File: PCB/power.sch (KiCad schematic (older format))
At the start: 46 parts, among them J801 V_IN, Q801 AOD4189, U801 ACS712xLCTR-20A, U802 NCP1117-5.0_SOT223, U803 L5973D, U804 NCP1117-3.3_SOT223

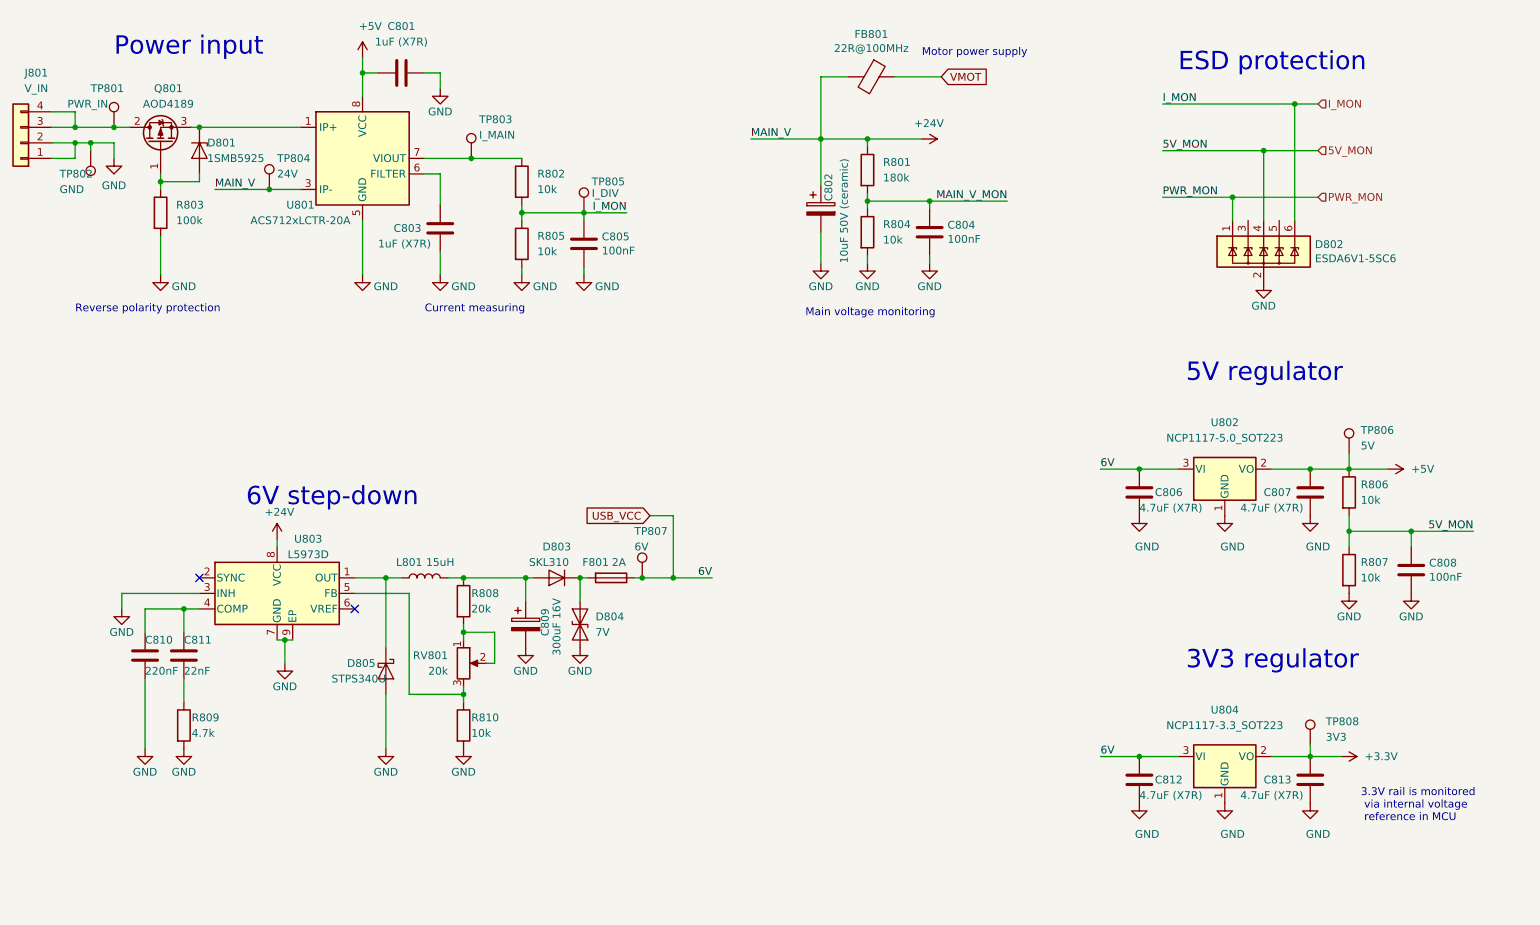
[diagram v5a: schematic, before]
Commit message: Schema: fix schema ERC, connect CS, FLAG and BUSY pins to MCU, connect SPI
ERC: fixed L6470 pin types, add power flags, fixed programming
connector pin types
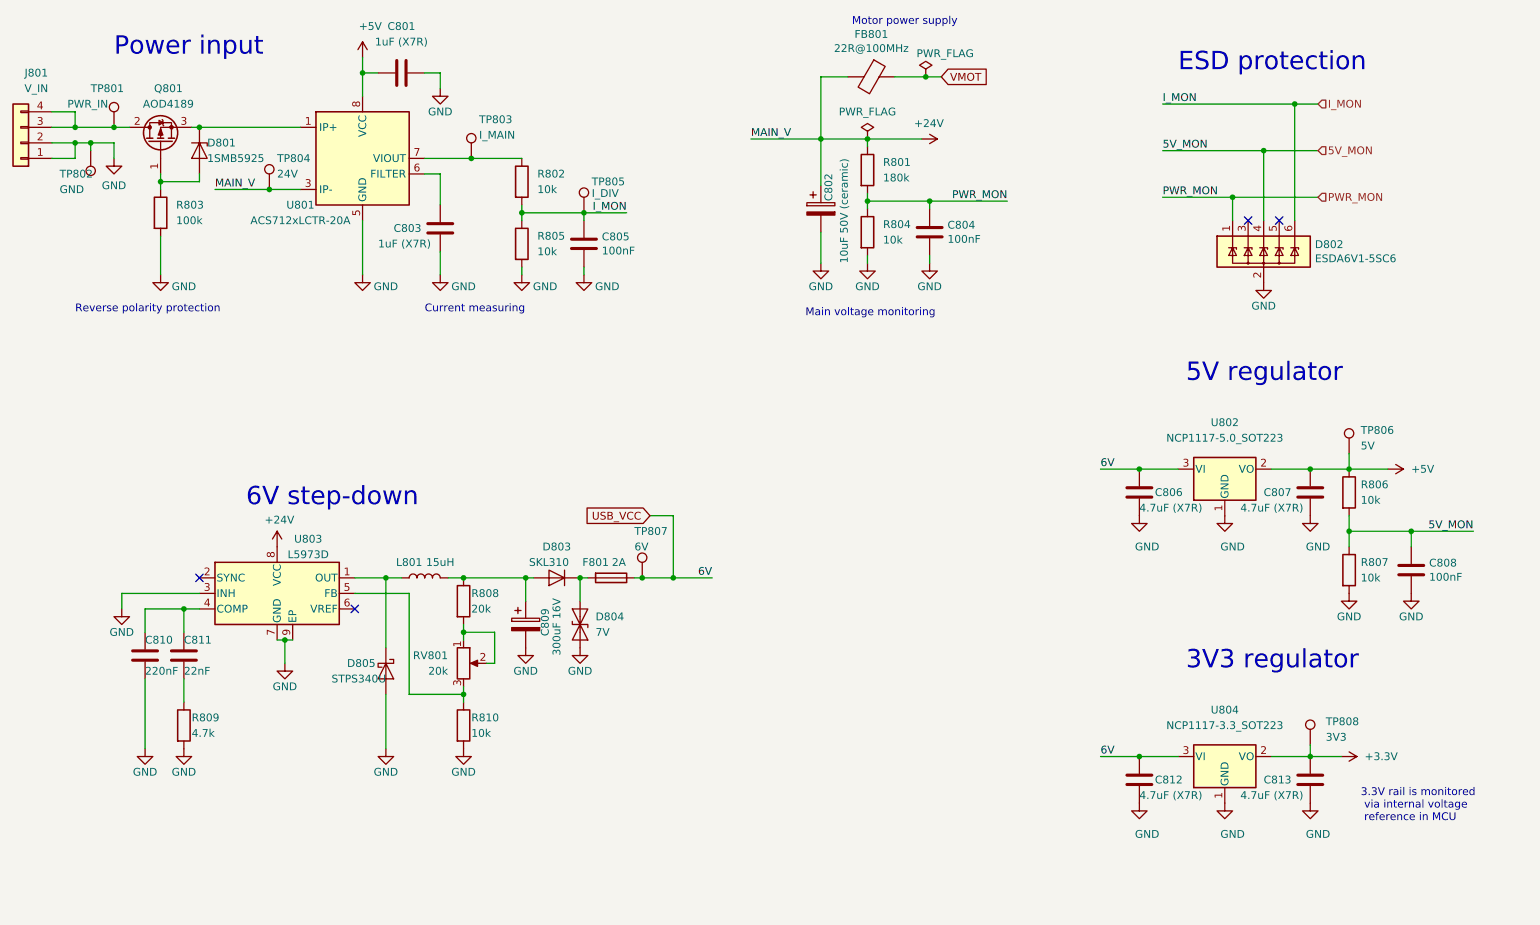
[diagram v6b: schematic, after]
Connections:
- net MAIN_V_MON is gone; now on net PWR_MON: C804.1, R801.2, R804.1
- no-connect marks 2 -> 4
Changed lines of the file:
@@
 	8900 1750 8450 1750
 Connection ~ 8900 1750
-Text Label 7450 1775 2    50   ~ 0
-MAIN_V_MON
-Text Label 8450 1750 0    50   ~ 0
-PWR_MON
 $Comp
 L Device:C C808
@@
 	3700 1500 4000 1500
 Wire Wire Line
-	2750 3950 2750 4000
-Wire Wire Line
 	8450 1150 9300 1150
 Wire Wire Line
@@
 VMOT
 Wire Wire Line
-	6725 975  7025 975
+	6725 975  6925 975
 Wire Wire Line
 	6950 1775 7450 1775
@@
 L power:+24V #PWR0818
 U 1 1 5D4903EF
-P 2750 3950
-F 0 "#PWR0818" H 2750 3800 50  0001 C CNN
-F 1 "+24V" H 2765 4123 50  0000 C CNN
-F 2 "" H 2750 3950 50  0001 C CNN
-F 3 "" H 2750 3950 50  0001 C CNN
-	1    2750 3950
+P 2750 4000
+F 0 "#PWR0818" H 2750 3850 50  0001 C CNN
+F 1 "+24V" H 2765 4173 50  0000 C CNN
+F 2 "" H 2750 4000 50  0001 C CNN
+F 3 "" H 2750 4000 50  0001 C CNN
+	1    2750 4000
 	1    0    0    -1
 $EndComp
@@
 Text Notes 6150 2525 0    50   ~ 0
 Main voltage monitoring
-Text Notes 6900 850  0    50   ~ 0
+Text Notes 6450 650  0    50   ~ 0
 Motor power supply
 Text Notes 3700 2500 0    50   ~ 0
@@
 Text Notes 9725 5775 0    50   ~ 0
 3.3V rail is monitored\n via internal voltage\n reference in MCU
+Text Label 8450 1750 0    50   ~ 0
+PWR_MON
+Text Label 7450 1775 2    50   ~ 0
+PWR_MON
+$Comp
+L power:PWR_FLAG #FLG0107
+U 1 1 5E41C5DC
+P 6925 975
+F 0 "#FLG0107" H 6925 1050 50  0001 C CNN
+F 1 "PWR_FLAG" H 7050 1125 50  0000 C CNN
+F 2 "" H 6925 975 50  0001 C CNN
+F 3 "~" H 6925 975 50  0001 C CNN
+	1    6925 975
+	1    0    0    -1
+$EndComp
+Connection ~ 6925 975
+Wire Wire Line
+	6925 975  7025 975
+NoConn ~ 9000 1900
+NoConn ~ 9200 1900
+$Comp
+L power:PWR_FLAG #FLG0109
+U 1 1 5E439F29
+P 6550 1375
+F 0 "#FLG0109" H 6550 1450 50  0001 C CNN
+F 1 "PWR_FLAG" H 6550 1550 50  0000 C CNN
+F 2 "" H 6550 1375 50  0001 C CNN
+F 3 "~" H 6550 1375 50  0001 C CNN
+	1    6550 1375
+	1    0    0    -1
+$EndComp
 $EndSCHEMATC

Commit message: PCB: route current meter, reverse polarity protection, stepdown converter
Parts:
- D802: footprint Package_TO_SOT_SMD:SOT-23-6 -> Package_DFN_QFN:ST_UQFN-6L_1.5x1.7mm_Pitch0.5mm
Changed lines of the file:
@@
 F 0 "D802" H 9430 2146 50  0000 L CNN
 F 1 "ESDA6V1-5SC6" H 9430 2055 50  0000 L CNN
-F 2 "Package_TO_SOT_SMD:SOT-23-6" H 9800 1850 50  0001 C CNN
+F 2 "Package_DFN_QFN:ST_UQFN-6L_1.5x1.7mm_Pitch0.5mm" H 9800 1850 50  0001 C CNN
 F 3 "www.st.com/resource/en/datasheet/esda6v1-5sc6.pdf" V 9100 2100 50  0001 C CNN
 	1    9100 2100

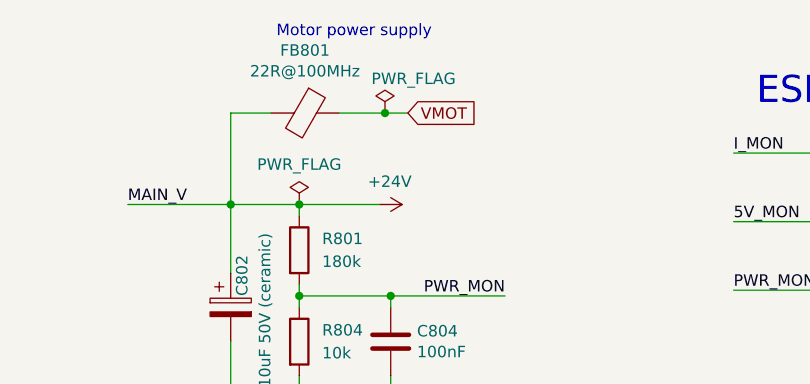
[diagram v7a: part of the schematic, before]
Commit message: PCB: upgrade power lines for VMOT (3mm -> 5mm), add second ferrite to VMOT
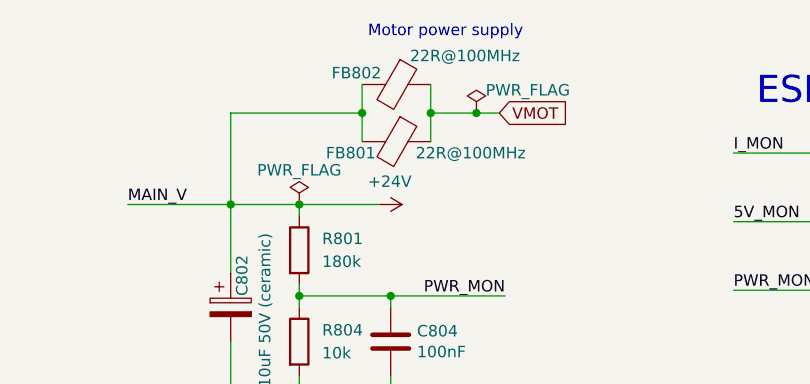
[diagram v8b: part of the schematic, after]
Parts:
- added FB802: 22R@100MHz, Inductor_SMD:L_0805_2012Metric, symbol Device:Ferrite_Bead
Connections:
- net +24V: now also FB802.2
- net VMOT: now also FB802.1
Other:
- moved on the sheet: FB801
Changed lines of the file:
@@
 L Device:Ferrite_Bead FB801
 U 1 1 5D478B04
-P 6575 975
-F 0 "FB801" V 6301 975 50  0000 C CNN
-F 1 "22R@100MHz" V 6392 975 50  0000 C CNN
-F 2 "Inductor_SMD:L_0805_2012Metric" V 6505 975 50  0001 C CNN
-F 3 "~" H 6575 975 50  0001 C CNN
-	1    6575 975
+P 6975 850
+F 0 "FB801" V 7275 650 50  0000 C CNN
+F 1 "22R@100MHz" V 7275 1175 50  0000 C CNN
+F 2 "Inductor_SMD:L_0805_2012Metric" V 6905 850 50  0001 C CNN
+F 3 "~" H 6975 850 50  0001 C CNN
+	1    6975 850
 	0    1    1    0
 $EndComp
-Text GLabel 7025 975  2    50   Input ~ 0
+Text GLabel 7425 975  2    50   Input ~ 0
 VMOT
 Wire Wire Line
-	6725 975  6925 975
+	7125 975  7325 975
 Wire Wire Line
 	6950 1775 7450 1775
@@
 Wire Wire Line
 	6250 1375 6250 975
-Wire Wire Line
-	6250 975  6425 975
 Text Notes 6150 2525 0    50   ~ 0
 Main voltage monitoring
-Text Notes 6450 650  0    50   ~ 0
+Text Notes 6850 650  0    50   ~ 0
 Motor power supply
 Text Notes 3700 2500 0    50   ~ 0
@@
 L power:PWR_FLAG #FLG0107
 U 1 1 5E41C5DC
-P 6925 975
-F 0 "#FLG0107" H 6925 1050 50  0001 C CNN
-F 1 "PWR_FLAG" H 7050 1125 50  0000 C CNN
-F 2 "" H 6925 975 50  0001 C CNN
-F 3 "~" H 6925 975 50  0001 C CNN
-	1    6925 975
-	1    0    0    -1
-$EndComp
-Connection ~ 6925 975
-Wire Wire Line
-	6925 975  7025 975
+P 7325 975
+F 0 "#FLG0107" H 7325 1050 50  0001 C CNN
+F 1 "PWR_FLAG" H 7550 1075 50  0000 C CNN
+F 2 "" H 7325 975 50  0001 C CNN
+F 3 "~" H 7325 975 50  0001 C CNN
+	1    7325 975
+	1    0    0    -1
+$EndComp
+Connection ~ 7325 975
+Wire Wire Line
+	7325 975  7425 975
 NoConn ~ 9000 1900
 NoConn ~ 9200 1900
@@
 P 6550 1375
 F 0 "#FLG0109" H 6550 1450 50  0001 C CNN
-F 1 "PWR_FLAG" H 6550 1550 50  0000 C CNN
+F 1 "PWR_FLAG" H 6550 1525 50  0000 C CNN
 F 2 "" H 6550 1375 50  0001 C CNN
 F 3 "~" H 6550 1375 50  0001 C CNN
@@
 	1    0    0    -1
 $EndComp
+Wire Wire Line
+	7125 975  7125 850
+Wire Wire Line
+	6825 850  6825 975
+Wire Wire Line
+	6250 975  6825 975
+$Comp
+L Device:Ferrite_Bead FB802
+U 1 1 5E547299
+P 6975 1100
+F 0 "FB802" V 6675 925 50  0000 C CNN
+F 1 "22R@100MHz" V 6600 1400 50  0000 C CNN
+F 2 "Inductor_SMD:L_0805_2012Metric" V 6905 1100 50  0001 C CNN
+F 3 "~" H 6975 1100 50  0001 C CNN
+	1    6975 1100
+	0    1    1    0
+$EndComp
+Wire Wire Line
+	7125 1100 7125 975
+Connection ~ 7125 975
+Wire Wire Line
+	6825 975  6825 1100
+Connection ~ 6825 975
 $EndSCHEMATC
